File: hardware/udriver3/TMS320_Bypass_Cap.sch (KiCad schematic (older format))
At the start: 24 parts

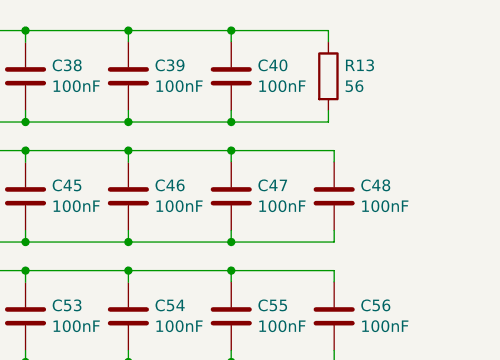
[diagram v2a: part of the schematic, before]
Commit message: Released version, with 4mils/4mils for track width and isolation on outer and inner layers 0.45mm for inner and outer annular ring 0.1mm for finished via drill (for Seeed studio increase to 0.2mm) + USB connector added
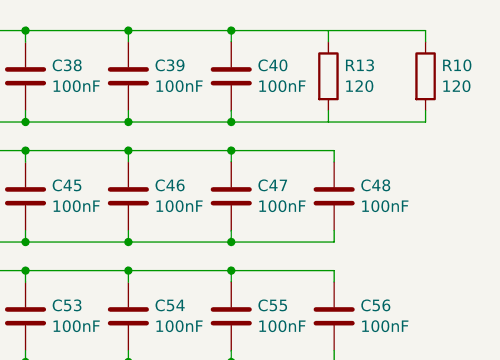
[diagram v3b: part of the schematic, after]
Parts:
- added R10: 120, Resistor_SMD:R_0201_0603Metric, symbol Device:R
- R13: value 56 -> 120; DigiKey P123082CT-ND -> P122692CT-ND; Farnell 2396848 -> 2396857; Mouser 667-ERJ-1GNF56R0C -> 667-ERJ-1GNF1200C; Part No ERJ-1GNF56R0C -> ERJ-1GNF1200C
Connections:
- net GND: now also R10.2
- net VDD_1V2: now also R10.1
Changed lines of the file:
@@
 AR Path="/5F3A3F16/5F5C1CF9/5F8FD7F1" Ref="R13"  Part="1"
 F 0 "R13" H 7695 3146 50  0000 L CNN
-F 1 "56" H 7695 3055 50  0000 L CNN
+F 1 "120" H 7695 3055 50  0000 L CNN
 F 2 "Resistor_SMD:R_0201_0603Metric" V 7555 3100 50  0001 C CNN
 F 3 "https://industrial.panasonic.com/cdbs/www-data/pdf/RDA0000/AOA0000C304.pdf" H 7625 3100 50  0001 C CNN
-F 4 "P123082CT-ND" H 7625 3100 50  0001 C CNN "DigiKey"
-F 5 "2396848" H 7625 3100 50  0001 C CNN "Farnell"
-F 6 "667-ERJ-1GNF56R0C" H 7625 3100 50  0001 C CNN "Mouser"
-F 7 "ERJ-1GNF56R0C" H 7625 3100 50  0001 C CNN "Part No"
+F 4 "P122692CT-ND" H 7625 3100 50  0001 C CNN "DigiKey"
+F 5 "2396857" H 7625 3100 50  0001 C CNN "Farnell"
+F 6 "667-ERJ-1GNF1200C" H 7625 3100 50  0001 C CNN "Mouser"
+F 7 "ERJ-1GNF1200C" H 7625 3100 50  0001 C CNN "Part No"
 	1    7625 3100
 	1    0    0    -1
@@
 Connection ~ 5850 4350
 Connection ~ 5850 3950
+$Comp
+L Device:R R?
+U 1 1 5FC1F8B3
+P 8050 3100
+AR Path="/5F3A3F16/5FC1F8B3" Ref="R?"  Part="1"
+AR Path="/5F3A3F16/5F5C1CF9/5FC1F8B3" Ref="R10"  Part="1"
+F 0 "R10" H 8120 3146 50  0000 L CNN
+F 1 "120" H 8120 3055 50  0000 L CNN
+F 2 "Resistor_SMD:R_0201_0603Metric" V 7980 3100 50  0001 C CNN
+F 3 "https://industrial.panasonic.com/cdbs/www-data/pdf/RDA0000/AOA0000C304.pdf" H 8050 3100 50  0001 C CNN
+F 4 "P122692CT-ND" H 8050 3100 50  0001 C CNN "DigiKey"
+F 5 "2396857" H 8050 3100 50  0001 C CNN "Farnell"
+F 6 "667-ERJ-1GNF1200C" H 8050 3100 50  0001 C CNN "Mouser"
+F 7 "ERJ-1GNF1200C" H 8050 3100 50  0001 C CNN "Part No"
+	1    8050 3100
+	1    0    0    -1
+$EndComp
+Wire Wire Line
+	8050 2950 8050 2900
+Wire Wire Line
+	8050 2900 7625 2900
+Wire Wire Line
+	7625 3300 8050 3300
+Wire Wire Line
+	8050 3300 8050 3250
 $EndSCHEMATC

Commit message: Release 1.1 - Update components values + BOM - Update of J1 pins affectation now matching J2 distribution. - Update gerber files with missing inner layers - Few updates of the PCB layout (J2 redraw + decoupling cap)
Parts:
- C34, C35, C36, C37, C38, C39, C40, C41, C42, C43, C44, C45, C46, C47, C48, C49, C50, C51, C52, C53, C54, C55, C56: DigiKey 490-14450-1-ND -> 490-14571-1-ND; Farnell 2990681 -> 3790414; Mouser 81-GRM033C71A104KE4D -> 81-GRM033R61E104KE4J; Part No GRM033C71A104KE14D -> GRM033R61E104KE14J; RS 185-1751 -> 185-2066
